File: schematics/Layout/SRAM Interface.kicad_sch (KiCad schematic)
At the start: 0 parts

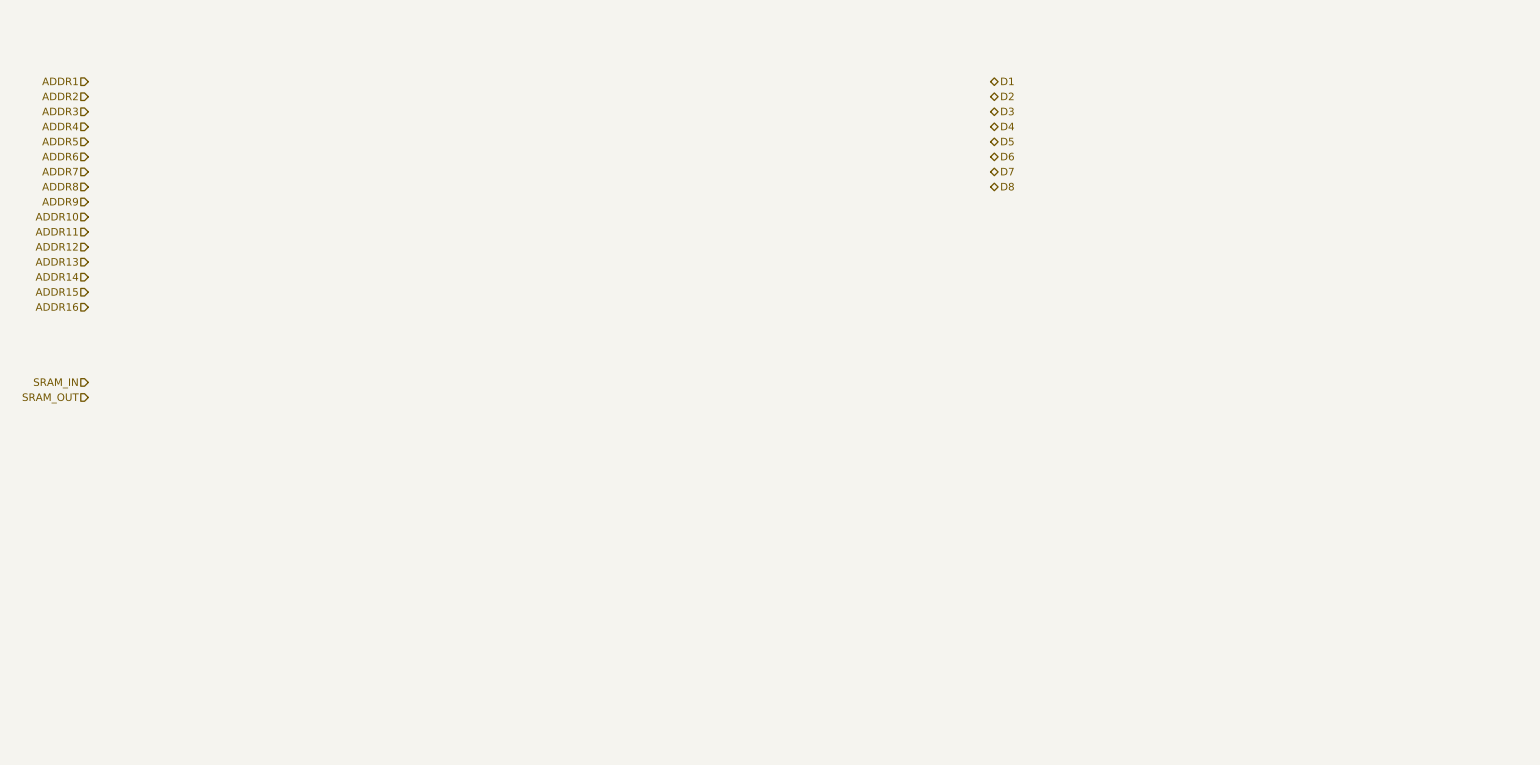
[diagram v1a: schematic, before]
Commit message: Update layout diagram with new boards in following places:  - Added buffer boards to all register boards.  - Fixed PC not getting address lines.  - Added SRAM interface boards.  - Updated to use Mini Control Signals Distributors.
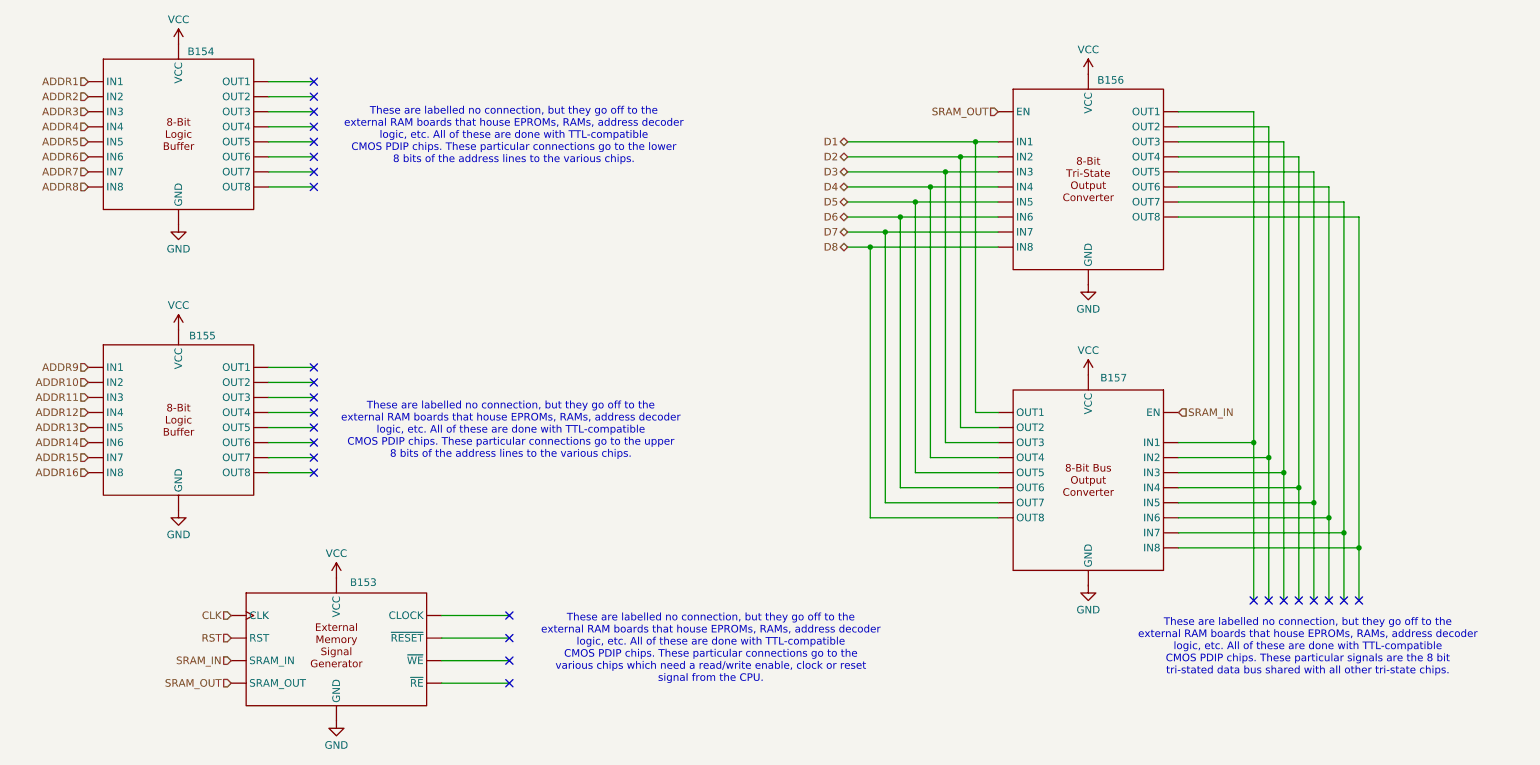
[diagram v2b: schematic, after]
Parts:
- added B153: ~, symbol MiniDragon:External Memory Signal Generator
- added B154, B155: ~, symbol MiniDragon:8-bit Logic Buffer
- added B156: ~, symbol MiniDragon:8-bit Tri-State Output
- added B157: ~, symbol MiniDragon:8-bit Bus Output
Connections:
- net ADDR1: now also B154. (OUT8)
- net ADDR10: now also B155. (OUT8)
- net ADDR11: now also B155. (OUT8)
- net ADDR12: now also B155. (OUT8)
- net ADDR13: now also B155. (OUT8)
- net ADDR14: now also B155. (OUT8)
- net ADDR15: now also B155. (OUT8)
- net ADDR16: now also B155. (OUT8)
- net ADDR2: now also B154. (OUT8)
- net ADDR3: now also B154. (OUT8)
- net ADDR4: now also B154. (OUT8)
- net ADDR5: now also B154. (OUT8)
- net ADDR6: now also B154. (OUT8)
- net ADDR7: now also B154. (OUT8)
- net ADDR8: now also B154. (OUT8)
- net ADDR9: now also B155. (OUT8)
- net D1: now also B156. (OUT8), B157. (OUT8)
- net D2: now also B156. (OUT8), B157. (OUT8)
- net D3: now also B156. (OUT8), B157. (OUT8)
- net D4: now also B156. (OUT8), B157. (OUT8)
- net D5: now also B156. (OUT8), B157. (OUT8)
- net D6: now also B156. (OUT8), B157. (OUT8)
- net D7: now also B156. (OUT8), B157. (OUT8)
- net D8: now also B156. (OUT8), B157. (OUT8)
- net SRAM_IN: now also B153. (~{RE}), B157. (OUT8)
- net SRAM_OUT: now also B153. (~{RE}), B156. (OUT8)
- new net: B156. (OUT8), B157. (OUT8) (x8)
- new net CLK: B153. (~{RE})
- new net GND: B153. (~{RE}), B154. (OUT8), B155. (OUT8), B156. (OUT8), B157. (OUT8)
- new net RST: B153. (~{RE})
- new net VCC: B153. (~{RE}), B154. (OUT8), B155. (OUT8), B156. (OUT8), B157. (OUT8)
- no-connect marks 0 -> 28
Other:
- note added: "These are labelled no connection, but they go off to the external RAM boards that house EPROMs, RAMs, address decoder logic, etc. All of these are done with TTL-compatible CMOS PDIP chips. These particular connections go to the lower 8 bits of the address lines to the various chips."
- note added: "These are labelled no connection, but they go off to the external RAM boards that house EPROMs, RAMs, address decoder logic, etc. All of these are done with TTL-compatible CMOS PDIP chips. These particular connections go to the upper 8 bits of the address lines to the various chips."
- note added: "These are labelled no connection, but they go off to the external RAM boards that house EPROMs, RAMs, address decoder logic, etc. All of these are done with TTL-compatible CMOS PDIP chips. These particular connections go to the various chips which need a read/write enable, clock or reset signal from the CPU."
- note added: "These are labelled no connection, but they go off to the external RAM boards that house EPROMs, RAMs, address decoder logic, etc. All of these are done with TTL-compatible CMOS PDIP chips. These particular signals are the 8 bit tri-stated data bus shared with all other tri-state chips."

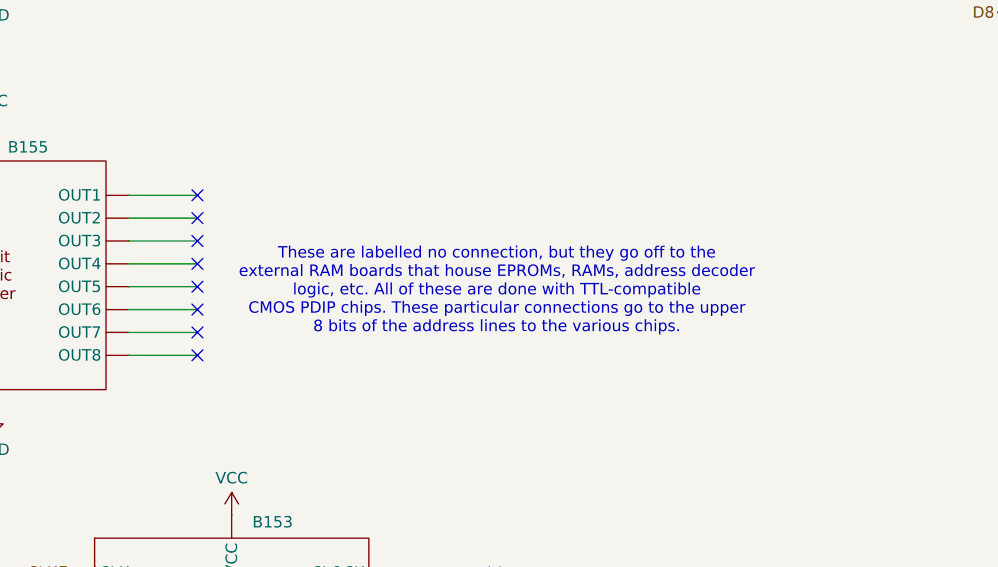
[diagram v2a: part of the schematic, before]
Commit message: Bugfix crossed connections on layout main data bus.
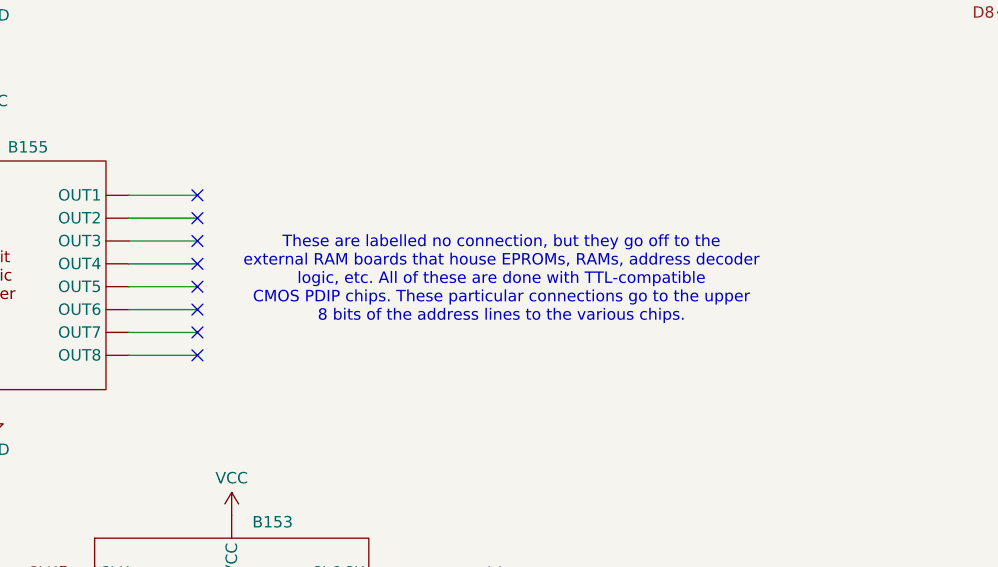
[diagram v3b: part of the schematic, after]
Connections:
- new net: B156. (OUT8), B157. (OUT8) (x8)
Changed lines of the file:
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@@
 	(text "These are labelled no connection, but they go off to the \nexternal RAM boards that house EPROMs, RAMs, address decoder\nlogic, etc. All of these are done with TTL-compatible\nCMOS PDIP chips. These particular connections go to the upper\n8 bits of the address lines to the various chips."
 		(exclude_from_sim no)
-		(at 109.474 84.328 0)
+		(at 109.982 83.058 0)
 		(effects
 			(font

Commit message: Update with new Shift symbol, diagram the rest of the ALU and more instruction decoder boards.
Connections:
- new net: B156. (OUT8), B157. (OUT8) (x8)
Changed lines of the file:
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@@
 	)
 	(symbol
-		(lib_name "8-bit Logic Buffer_1")
 		(lib_id "MiniDragon:8-bit Logic Buffer")
 		(at 53.34 82.55 0)
@@
 	)
 	(symbol
+		(lib_name "8-bit Logic Buffer_1")
 		(lib_id "MiniDragon:8-bit Logic Buffer")
 		(at 53.34 34.29 0)

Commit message: Documentation updates
Update README with newly discovered eratta.
Update PCBs directory to include 3 newer PCBs that were missing.
Update layout to reflect SHL/SHR stability fixes.
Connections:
- new net: B156. (OUT8), B157. (OUT8) (x8)
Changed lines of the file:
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@@
 		)
 		(instances
-			(project ""
+			(project "MiniDragon"
 				(path "/5049efcd-4f75-45d1-9c4f-a0a8d8f08d5b/a0907723-5fb1-4efb-90f1-494907708bae"
 					(reference "B157")
@@
 		)
 		(instances
-			(project ""
+			(project "MiniDragon"
 				(path "/5049efcd-4f75-45d1-9c4f-a0a8d8f08d5b/a0907723-5fb1-4efb-90f1-494907708bae"
 					(reference "B153")
@@
 		)
 		(instances
-			(project ""
+			(project "MiniDragon"
 				(path "/5049efcd-4f75-45d1-9c4f-a0a8d8f08d5b/a0907723-5fb1-4efb-90f1-494907708bae"
 					(reference "B156")
@@
 		)
 		(instances
-			(project ""
+			(project "MiniDragon"
 				(path "/5049efcd-4f75-45d1-9c4f-a0a8d8f08d5b/a0907723-5fb1-4efb-90f1-494907708bae"
 					(reference "B154")
